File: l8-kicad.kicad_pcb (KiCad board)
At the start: 4 copper layers, 55.5 x 89.5 mm, 110 parts, among them J1 USB_B_Mini, J2 LCD 3.2" 240x320 Conn_01x14_P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, J3 Screw_Terminal_01x06, J4 Conn_ST_STDC14, J5 Conn_02x20_Odd_Even, J7 TC2030 - TAG Connect, Q1 SI2301CDS-T1-GE3, Q4 SI2301CDS-T1-GE3, Q5 SI2301CDS-T1-GE3, SW1 SW_Push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

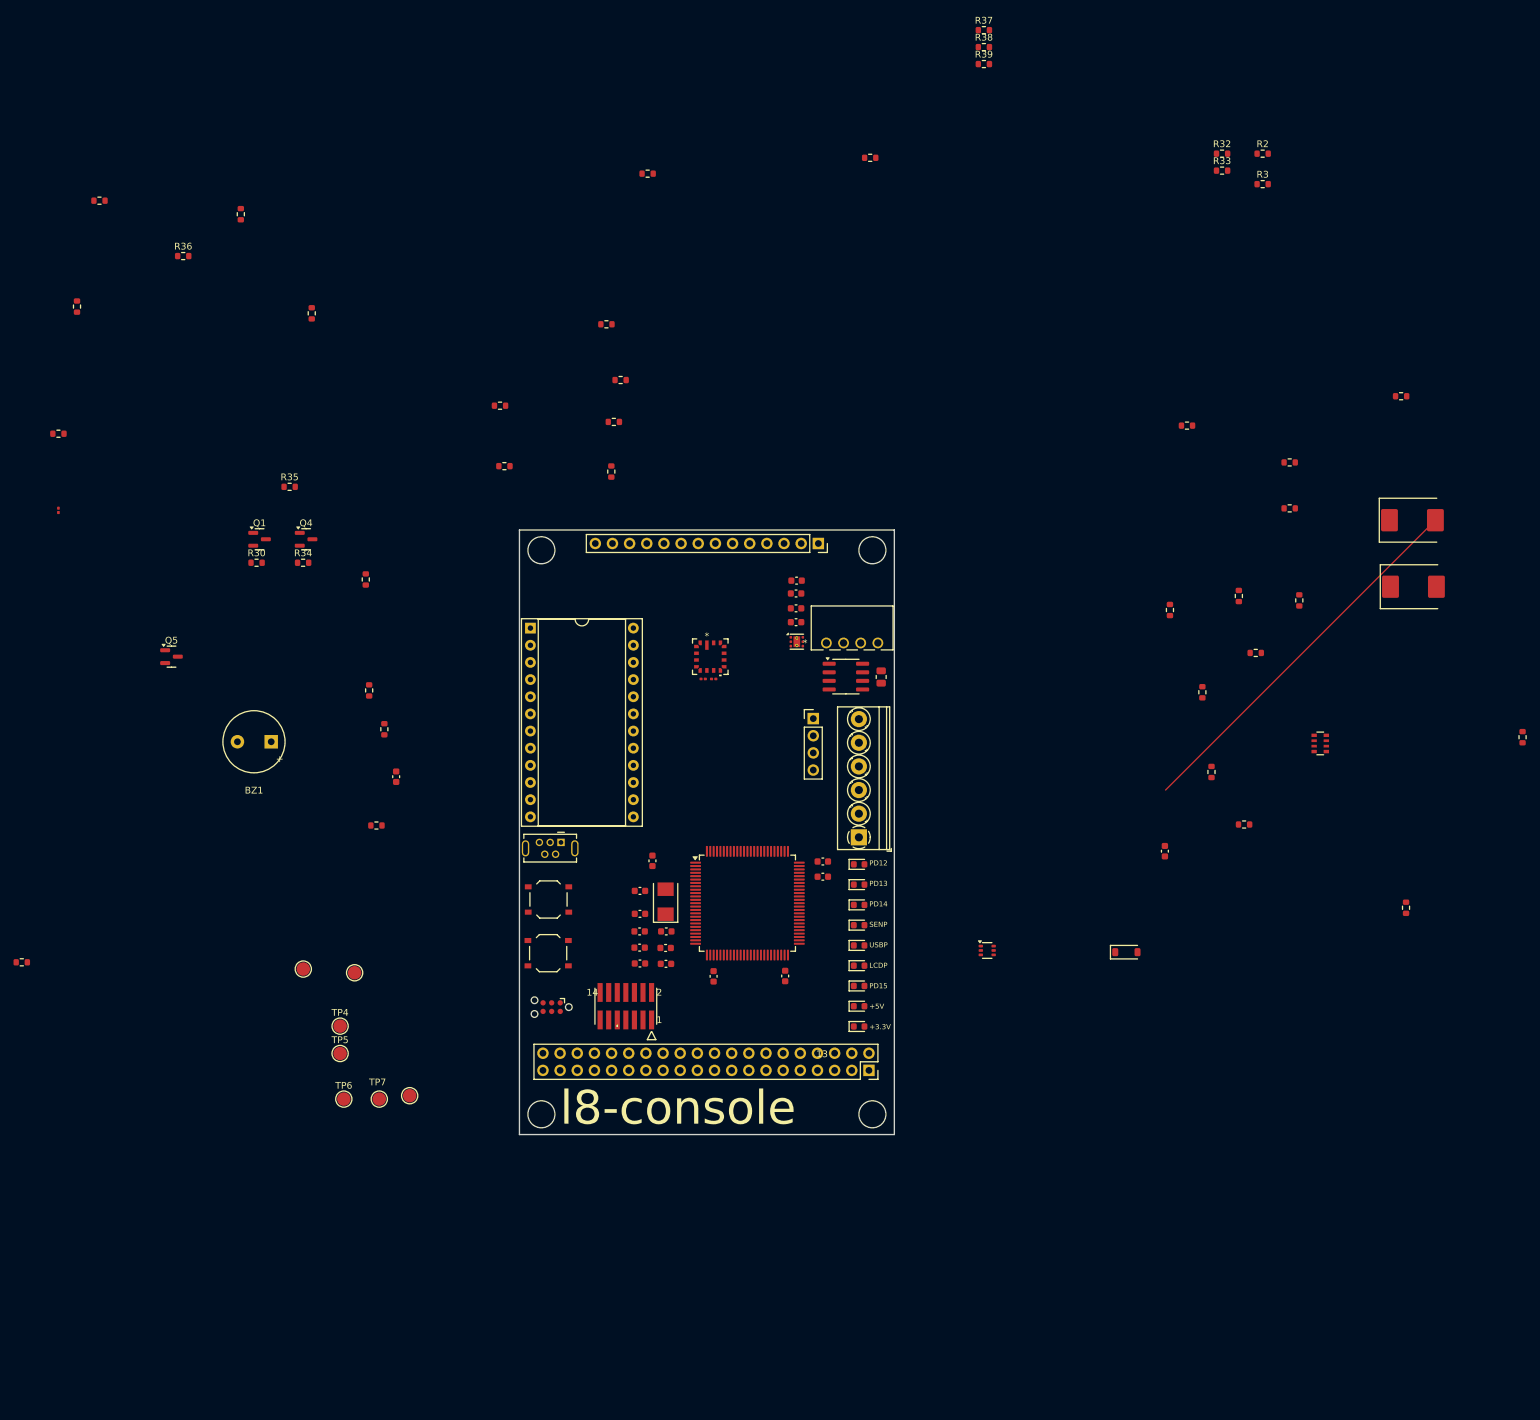
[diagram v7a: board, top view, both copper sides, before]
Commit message: changed to tp and subbed to quilter
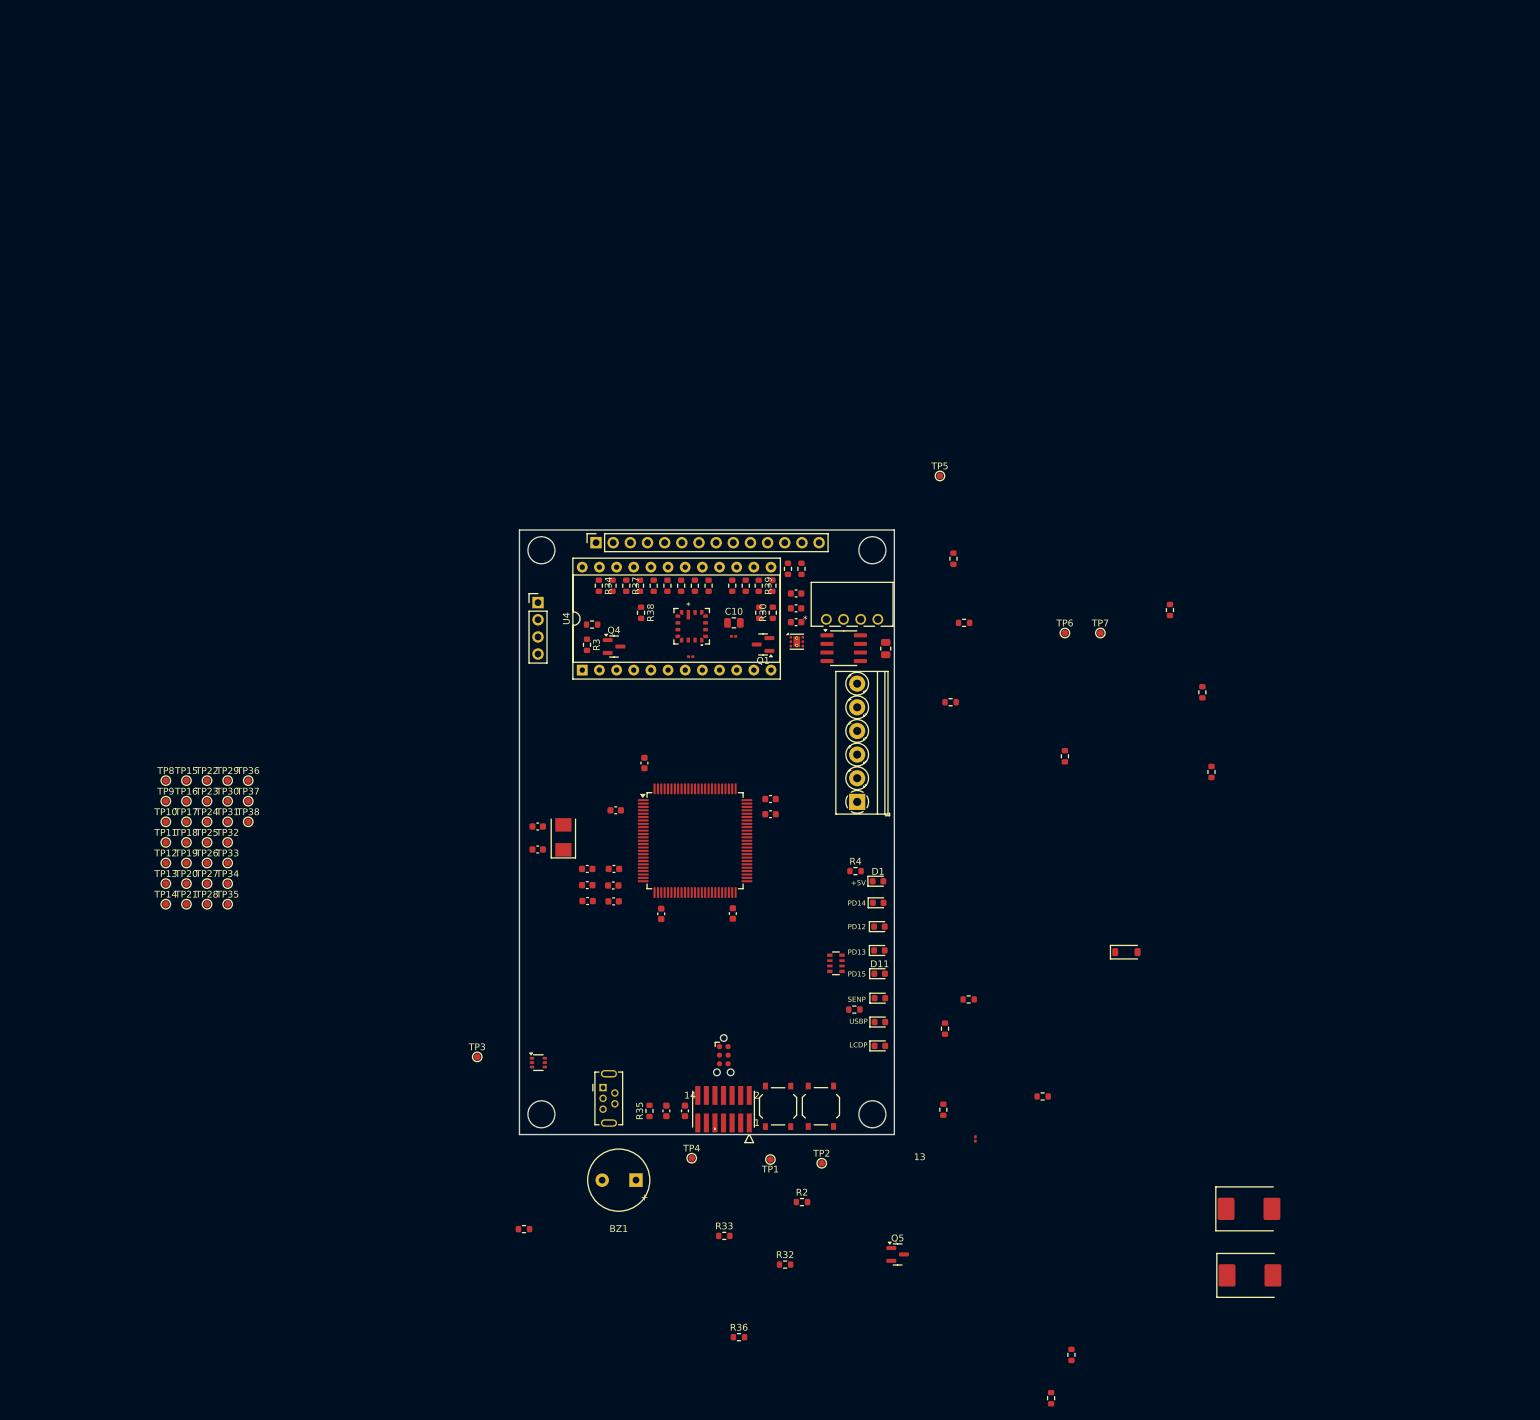
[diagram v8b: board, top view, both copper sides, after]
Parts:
- removed D7: LED-RED, LED_SMD:LED_0603_1608Metric
- removed J5: Conn_02x20_Odd_Even, Connector_PinSocket_2.54mm:PinSocket_2x20_P2.54mm_Vertical
- removed R16: 1k, Resistor_SMD:R_0603_1608Metric
- added C10: 10uF, Capacitor_SMD:C_0805_2012Metric, F.Cu at (131.8, 113.8)
- added TP10: PC8, TestPoint:TestPoint_Pad_D1.0mm, F.Cu at (47.6, 143.2)
- added TP11: PC9, TestPoint:TestPoint_Pad_D1.0mm, F.Cu at (47.6, 146.2)
- added TP12: PC13, TestPoint:TestPoint_Pad_D1.0mm, F.Cu at (47.6, 149.3)
- added TP13: PC14, TestPoint:TestPoint_Pad_D1.0mm, F.Cu at (47.6, 152.3)
- added TP14: PC15, TestPoint:TestPoint_Pad_D1.0mm, F.Cu at (47.6, 155.4)
- added TP15: PC0, TestPoint:TestPoint_Pad_D1.0mm, F.Cu at (50.7, 137.1)
- added TP16: PA0, TestPoint:TestPoint_Pad_D1.0mm, F.Cu at (50.7, 140.2)
- added TP17: PA1, TestPoint:TestPoint_Pad_D1.0mm, F.Cu at (50.7, 143.2)
- added TP18: PA4, TestPoint:TestPoint_Pad_D1.0mm, F.Cu at (50.7, 146.2)
- added TP19: PA8, TestPoint:TestPoint_Pad_D1.0mm, F.Cu at (50.7, 149.3)
- added TP20: PB4, TestPoint:TestPoint_Pad_D1.0mm, F.Cu at (50.7, 152.3)
- added TP21: PB5, TestPoint:TestPoint_Pad_D1.0mm, F.Cu at (50.7, 155.4)
- added TP22: PB8, TestPoint:TestPoint_Pad_D1.0mm, F.Cu at (53.8, 137.1)
- added TP23: PB9, TestPoint:TestPoint_Pad_D1.0mm, F.Cu at (53.8, 140.2)
- added TP24: PB10, TestPoint:TestPoint_Pad_D1.0mm, F.Cu at (53.8, 143.2)
- added TP25: PB11, TestPoint:TestPoint_Pad_D1.0mm, F.Cu at (53.8, 146.2)
- added TP26: PB12, TestPoint:TestPoint_Pad_D1.0mm, F.Cu at (53.8, 149.3)
- added TP27: PD15, TestPoint:TestPoint_Pad_D1.0mm, F.Cu at (53.8, 152.3)
- added TP28: PD14, TestPoint:TestPoint_Pad_D1.0mm, F.Cu at (53.8, 155.4)
- added TP29: PD13, TestPoint:TestPoint_Pad_D1.0mm, F.Cu at (56.8, 137.1)
- added TP30: PD12, TestPoint:TestPoint_Pad_D1.0mm, F.Cu at (56.8, 140.2)
- added TP31: PE8, TestPoint:TestPoint_Pad_D1.0mm, F.Cu at (56.8, 143.2)
- added TP32: PE7, TestPoint:TestPoint_Pad_D1.0mm, F.Cu at (56.8, 146.2)
- added TP33: PE0, TestPoint:TestPoint_Pad_D1.0mm, F.Cu at (56.8, 149.3)
- added TP34: PE1, TestPoint:TestPoint_Pad_D1.0mm, F.Cu at (56.8, 152.3)
- added TP35: PE9, TestPoint:TestPoint_Pad_D1.0mm, F.Cu at (56.8, 155.4)
- added TP36: PE10, TestPoint:TestPoint_Pad_D1.0mm, F.Cu at (59.9, 137.1)
- added TP37: PE11, TestPoint:TestPoint_Pad_D1.0mm, F.Cu at (59.9, 140.2)
- added TP38: PE12, TestPoint:TestPoint_Pad_D1.0mm, F.Cu at (59.9, 143.2)
- added TP8: PC6, TestPoint:TestPoint_Pad_D1.0mm, F.Cu at (47.6, 137.1)
- added TP9: PC7, TestPoint:TestPoint_Pad_D1.0mm, F.Cu at (47.6, 140.2)
- R48: value 2.2k -> 1K
- TP1, TP2, TP3, TP4, TP5, TP6, TP7: footprint TestPoint:TestPoint_Pad_D2.0mm -> TestPoint:TestPoint_Pad_D1.0mm
- moved R10 213.9 mm to (181.7, 222.1)
- moved R9 194.4 mm to (178.7, 228.5)
- moved R36 180.0 mm to (132.5, 219.5)
- moved R32 176.7 mm to (139.3, 208.8)
- moved R33 174.1 mm to (130.3, 204.5)
- moved R2 169.5 mm to (141.8, 199.5)
- moved R8 168.5 mm to (162.8, 185.8)
- moved FB1 164.6 mm to (167.5, 190.2)
- moved Q5 139.2 mm to (156.0, 207.2)
- moved R31 130.0 mm to (177.5, 183.9)
- moved TP6 127.1 mm to (180.8, 115.2)
- moved TP7 127.1 mm to (186.0, 115.2)
- moved TP5 123.3 mm to (162.2, 92.0)
- moved R3 121.1 mm to (110.0, 117.0), turned to -90 degrees
- moved R21 109.6 mm to (141.8, 105.8)
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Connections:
- D1 pad 2: +3.3V -> Net-(D1-A)
- D2 pad 1: Net-(D2-K) -> Net-(D1-A)
- D3 pad 1: Net-(D2-K) -> Net-(D1-A)
- PS1 pad 3: Net-(D2-K) -> Net-(D1-A)
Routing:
- net /VBATT: track 56.5 -> 0.00 mm
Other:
- board text removed: "+3.3V"
- board text removed: "l8-console"
